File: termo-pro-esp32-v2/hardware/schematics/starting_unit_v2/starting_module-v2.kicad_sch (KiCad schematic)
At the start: 18 parts, among them J1 Screw_Terminal_01x02, J2 Screw_Terminal_01x02, J3 Conn_01x08_Pin, K1 SANYOU_SRD_Form_C, Q1 PN2222A, SW1 SW_Push_LED, U2 ESP32-C3_SUPERMINI_TH

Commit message: Removed circular LED and replaced them with rectangular ones.
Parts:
- D1, D2: footprint LED_THT:LED_D5.0mm_FlatTop -> LED_THT:LED_Rectangular_W5.0mm_H2.0mm
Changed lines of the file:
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@@
 			)
 		)
-		(property "Footprint" "LED_THT:LED_D5.0mm_FlatTop"
+		(property "Footprint" "LED_THT:LED_Rectangular_W5.0mm_H2.0mm"
 			(at 171.45 78.74 0)
 			(hide yes)
@@
 			)
 		)
-		(property "Footprint" "LED_THT:LED_D5.0mm_FlatTop"
+		(property "Footprint" "LED_THT:LED_Rectangular_W5.0mm_H2.0mm"
 			(at 180.34 78.74 0)
 			(hide yes)

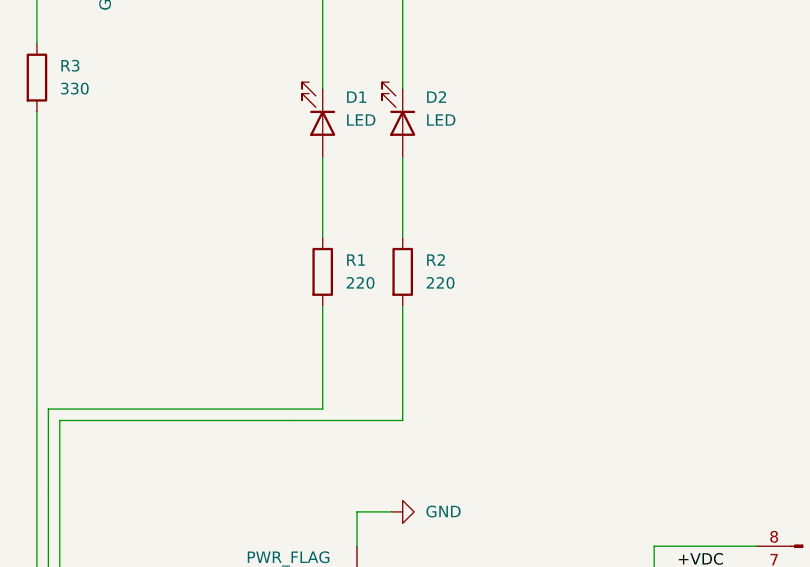
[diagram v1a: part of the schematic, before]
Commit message: Documentation changes
Starting unit schematic and PCB has been updated for the 50 ohm resistors used for LED.
gerber and drill files generated again.
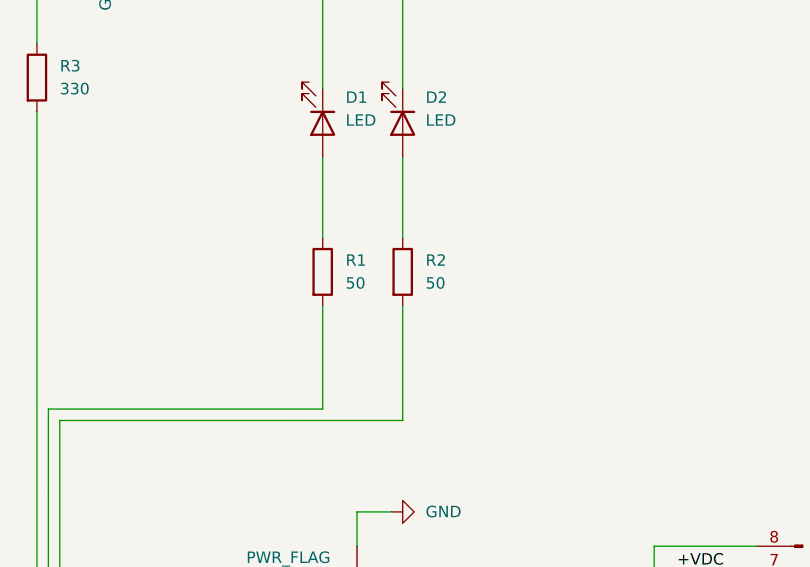
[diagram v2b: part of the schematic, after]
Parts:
- R1, R2: value 220 -> 50
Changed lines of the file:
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@@
 			)
 		)
-		(property "Value" "220"
+		(property "Value" "50"
 			(at 182.88 96.5199 0)
 			(show_name no)
@@
 			)
 		)
-		(property "Value" "220"
+		(property "Value" "50"
 			(at 173.99 96.5199 0)
 			(show_name no)
